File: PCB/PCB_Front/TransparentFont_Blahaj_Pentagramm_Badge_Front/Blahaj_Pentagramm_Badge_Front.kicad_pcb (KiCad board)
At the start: 2 copper layers, 79.8 x 79.8 mm, 13 parts

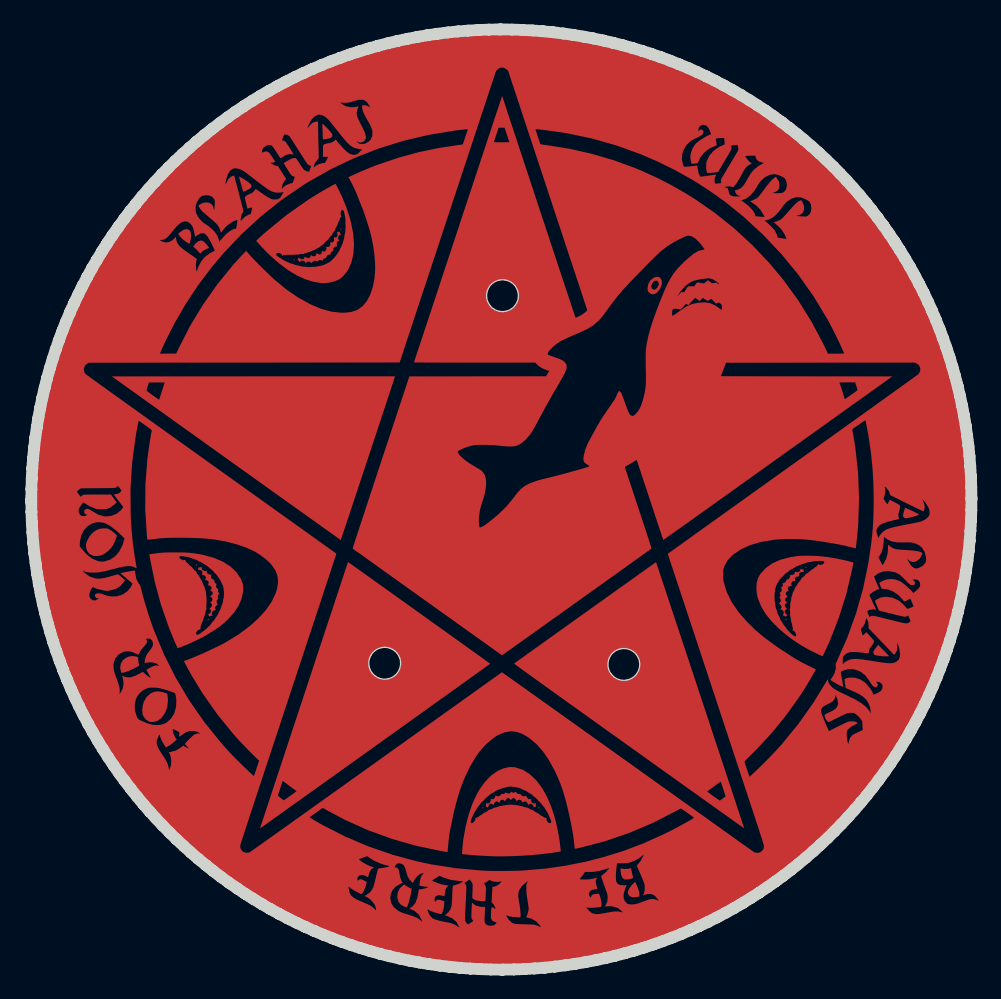
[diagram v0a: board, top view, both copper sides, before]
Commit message: Production Samples
TODO: Border for working sample to narrow.
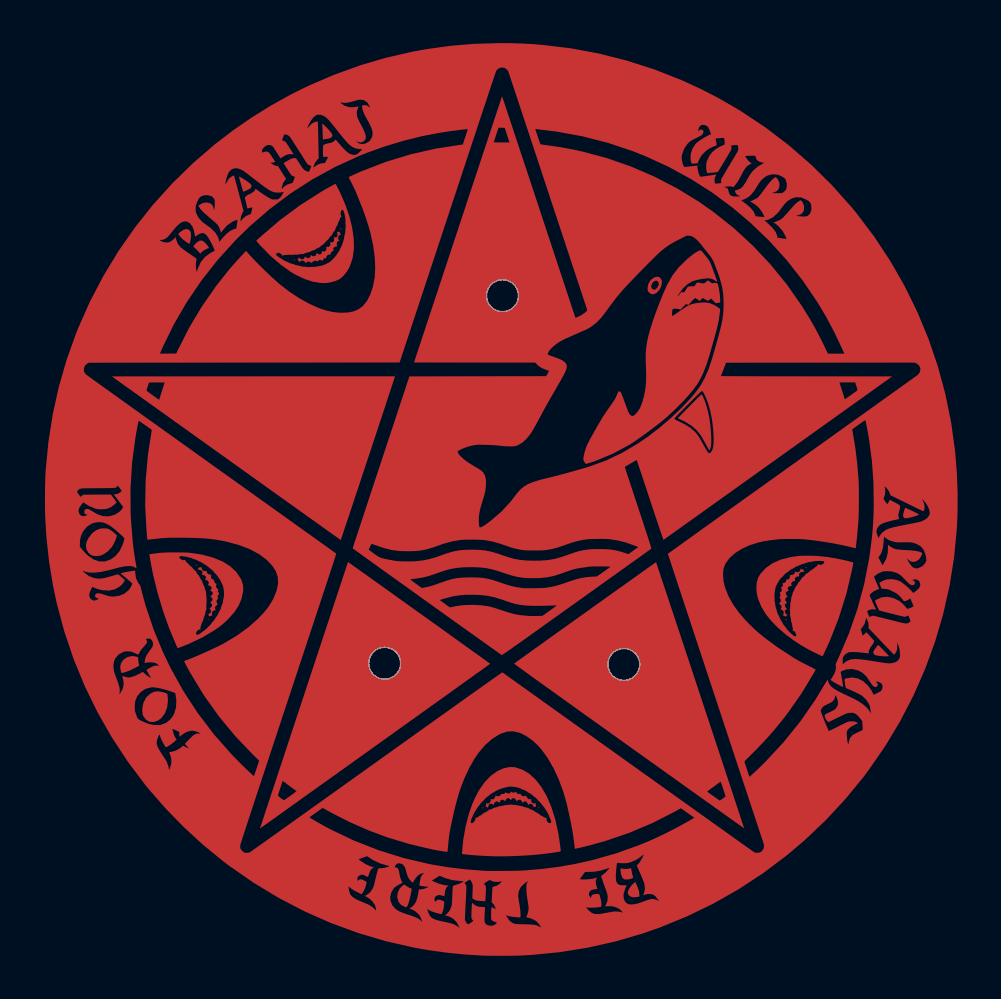
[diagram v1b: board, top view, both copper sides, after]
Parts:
- removed the ? at (100.0, 100.0) (x2)
- added ? (x14): , Graphics, F.Cu at (100.0, 100.0)
- added ? (x4): , Graphics, B.Cu at (100.0, 100.0)
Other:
- board outline removed

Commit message: Back corrections, Front Edge Cut bigger.
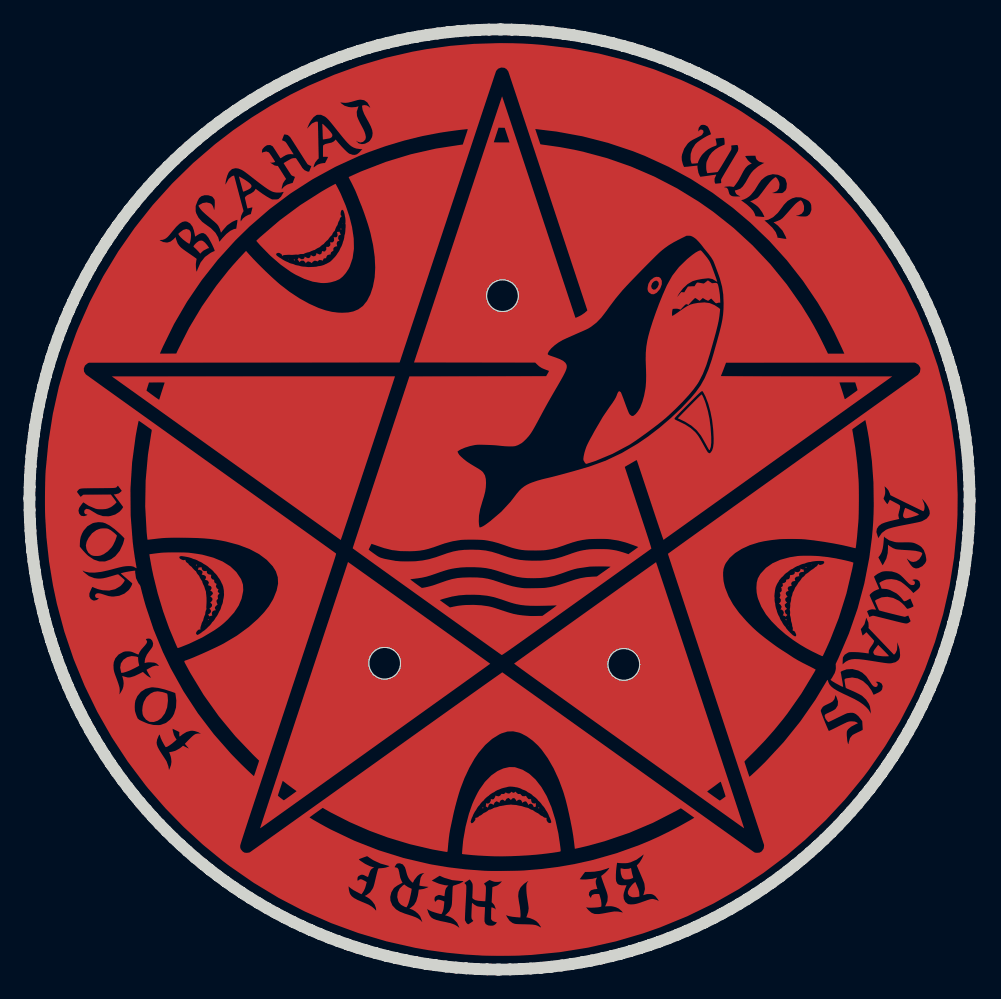
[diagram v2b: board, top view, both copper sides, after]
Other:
- board outline added: 79.8 x 79.8 mm
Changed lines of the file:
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@@
 			(drillshape 0)
 			(scaleselection 1)
-			(outputdirectory "production/")
+			(outputdirectory "production/Front_transparent/")
 		)
 	)
@@
 		(attr board_only exclude_from_pos_files exclude_from_bom)
 	)
+	(gr_poly
+		(pts
+			(xy 179.645 139.9) (xy 179.635 139.011) (xy 179.606 138.127) (xy 179.558 137.248) (xy 179.491 136.374)
+			(xy 179.406 135.505) (xy 179.302 134.642) (xy 179.179 133.785) (xy 179.039 132.934) (xy 178.881 132.088)
+			(xy 178.705 131.25) (xy 178.511 130.417) (xy 178.301 129.592) (xy 178.073 128.773) (xy 177.828 127.962)
+			(xy 177.567 127.158) (xy 177.289 126.361) (xy 176.996 125.573) (xy 176.686 124.792) (xy 176.36 124.02)
+			(xy 176.018 123.255) (xy 175.661 122.5) (xy 175.289 121.753) (xy 174.902 121.015) (xy 174.5 120.286)
+			(xy 174.083 119.567) (xy 173.652 118.857) (xy 173.206 118.158) (xy 172.747 117.468) (xy 172.273 116.788)
+			(xy 171.786 116.118) (xy 171.286 115.46) (xy 170.772 114.812) (xy 170.246 114.175) (xy 169.706 113.549)
+			(xy 169.154 112.934) (xy 168.589 112.331) (xy 168.012 111.74) (xy 167.424 111.161) (xy 166.823 110.594)
+			(xy 166.211 110.04) (xy 165.587 109.498) (xy 164.952 108.969) (xy 164.306 108.453) (xy 163.649 107.95)
+			(xy 162.982 107.461) (xy 162.304 106.985) (xy 161.616 106.523) (xy 160.918 106.075) (xy 160.21 105.641)
+			(xy 159.492 105.221) (xy 158.765 104.817) (xy 158.029 104.426) (xy 157.284 104.051) (xy 156.53 103.692)
+			(xy 155.767 103.347) (xy 154.996 103.019) (xy 154.217 102.706) (xy 153.43 102.409) (xy 152.635 102.128)
+			(xy 151.832 101.864) (xy 151.022 101.616) (xy 150.205 101.385) (xy 149.381 101.171) (xy 148.55 100.975)
+			(xy 147.712 100.795) (xy 146.868 100.634) (xy 146.018 100.49) (xy 145.162 100.365) (xy 144.3 100.257)
+			(xy 143.432 100.168) (xy 142.559 100.098) (xy 141.681 100.046) (xy 140.798 100.014) (xy 139.91 100)
+			(xy 139.745 100) (xy 138.856 100.01) (xy 137.972 100.039) (xy 137.093 100.087) (xy 136.219 100.154)
+			(xy 135.35 100.239) (xy 134.487 100.343) (xy 133.63 100.466) (xy 132.779 100.606) (xy 131.933 100.764)
+			(xy 131.095 100.94) (xy 130.262 101.134) (xy 129.437 101.344) (xy 128.618 101.572) (xy 127.807 101.817)
+			(xy 127.003 102.078) (xy 126.206 102.356) (xy 125.418 102.649) (xy 124.637 102.959) (xy 123.865 103.285)
+			(xy 123.1 103.627) (xy 122.345 103.984) (xy 121.598 104.356) (xy 120.86 104.743) (xy 120.131 105.145)
+			(xy 119.412 105.562) (xy 118.702 105.993) (xy 118.003 106.439) (xy 117.313 106.898) (xy 116.633 107.372)
+			(xy 115.963 107.859) (xy 115.305 108.359) (xy 114.657 108.873) (xy 114.02 109.399) (xy 113.394 109.939)
+			(xy 112.779 110.491) (xy 112.177 111.056) (xy 111.585 111.632) (xy 111.006 112.221) (xy 110.44 112.822)
+			(xy 109.885 113.434) (xy 109.343 114.058) (xy 108.814 114.693) (xy 108.298 115.339) (xy 107.795 115.996)
+			(xy 107.306 116.663) (xy 106.83 117.341) (xy 106.368 118.029) (xy 105.92 118.727) (xy 105.486 119.435)
+			(xy 105.066 120.153) (xy 104.662 120.88) (xy 104.272 121.616) (xy 103.896 122.361) (xy 103.537 123.115)
+			(xy 103.192 123.878) (xy 102.864 124.649) (xy 102.551 125.428) (xy 102.254 126.215) (xy 101.973 127.01)
+			(xy 101.709 127.813) (xy 101.461 128.623) (xy 101.23 129.44) (xy 101.016 130.264) (xy 100.82 131.095)
+			(xy 100.641 131.933) (xy 100.479 132.777) (xy 100.335 133.627) (xy 100.21 134.483) (xy 100.102 135.345)
+			(xy 100.013 136.213) (xy 99.943 137.086) (xy 99.891 137.964) (xy 99.859 138.847) (xy 99.845 139.735)
+			(xy 99.845 139.9) (xy 99.855 140.789) (xy 99.884 141.673) (xy 99.932 142.552) (xy 99.999 143.426)
+			(xy 100.084 144.295) (xy 100.188 145.158) (xy 100.311 146.015) (xy 100.451 146.866) (xy 100.609 147.711)
+			(xy 100.785 148.55) (xy 100.979 149.383) (xy 101.189 150.208) (xy 101.417 151.027) (xy 101.662 151.838)
+			(xy 101.923 152.642) (xy 102.201 153.438) (xy 102.494 154.227) (xy 102.804 155.008) (xy 103.13 155.78)
+			(xy 103.472 156.545) (xy 103.829 157.3) (xy 104.201 158.047) (xy 104.588 158.785) (xy 104.99 159.513)
+			(xy 105.407 160.233) (xy 105.838 160.942) (xy 106.284 161.642) (xy 106.743 162.332) (xy 107.217 163.012)
+			(xy 107.704 163.681) (xy 108.204 164.34) (xy 108.718 164.988) (xy 109.244 165.625) (xy 109.784 166.251)
+			(xy 110.336 166.866) (xy 110.901 167.468) (xy 111.477 168.059) (xy 112.066 168.639) (xy 112.667 169.205)
+			(xy 113.279 169.76) (xy 113.903 170.302) (xy 114.538 170.831) (xy 115.184 171.347) (xy 115.841 171.85)
+			(xy 116.508 172.339) (xy 117.186 172.815) (xy 117.874 173.277) (xy 118.572 173.725) (xy 119.28 174.159)
+			(xy 119.998 174.579) (xy 120.725 174.983) (xy 121.461 175.373) (xy 122.206 175.748) (xy 122.96 176.108)
+			(xy 123.723 176.453) (xy 124.494 176.781) (xy 125.273 177.094) (xy 126.06 177.391) (xy 126.855 177.672)
+			(xy 127.658 177.936) (xy 128.468 178.184) (xy 129.285 178.415) (xy 130.109 178.629) (xy 130.94 178.825)
+			(xy 131.778 179.004) (xy 132.622 179.166) (xy 133.472 179.31) (xy 134.328 179.435) (xy 135.19 179.543)
+			(xy 136.058 179.632) (xy 136.931 179.702) (xy 137.809 179.754) (xy 138.692 179.786) (xy 139.58 179.8)
+			(xy 139.745 179.8) (xy 140.634 179.79) (xy 141.518 179.761) (xy 142.397 179.713) (xy 143.271 179.646)
+			(xy 144.14 179.561) (xy 145.003 179.457) (xy 145.86 179.334) (xy 146.711 179.194) (xy 147.557 179.036)
+			(xy 148.395 178.86) (xy 149.228 178.666) (xy 150.053 178.456) (xy 150.872 178.228) (xy 151.683 177.983)
+			(xy 152.487 177.722) (xy 153.283 177.444) (xy 154.072 177.151) (xy 154.853 176.84) (xy 155.625 176.515)
+			(xy 156.39 176.173) (xy 157.145 175.816) (xy 157.892 175.444) (xy 158.63 175.057) (xy 159.358 174.655)
+			(xy 160.078 174.238) (xy 160.787 173.807) (xy 161.487 173.361) (xy 162.177 172.902) (xy 162.857 172.428)
+			(xy 163.527 171.941) (xy 164.185 171.441) (xy 164.833 170.927) (xy 165.47 170.401) (xy 166.096 169.861)
+			(xy 166.711 169.309) (xy 167.313 168.744) (xy 167.905 168.167) (xy 168.484 167.579) (xy 169.05 166.978)
+			(xy 169.605 166.366) (xy 170.147 165.742) (xy 170.676 165.107) (xy 171.192 164.461) (xy 171.695 163.804)
+			(xy 172.184 163.137) (xy 172.66 162.459) (xy 173.122 161.771) (xy 173.57 161.073) (xy 174.004 160.365)
+			(xy 174.424 159.647) (xy 174.828 158.92) (xy 175.218 158.184) (xy 175.593 157.439) (xy 175.953 156.685)
+			(xy 176.298 155.922) (xy 176.626 155.151) (xy 176.939 154.372) (xy 177.236 153.585) (xy 177.517 152.79)
+			(xy 177.781 151.987) (xy 178.029 151.177) (xy 178.26 150.36) (xy 178.474 149.536) (xy 178.67 148.705)
+			(xy 178.849 147.867) (xy 179.011 147.023) (xy 179.155 146.173) (xy 179.28 145.317) (xy 179.388 144.455)
+			(xy 179.477 143.587) (xy 179.547 142.714) (xy 179.599 141.836) (xy 179.631 140.953) (xy 179.645 140.065)
+			(xy 179.645 139.9)
+		)
+		(stroke
+			(width 1)
+			(type solid)
+		)
+		(fill none)
+		(layer "Edge.Cuts")
+	)
 )

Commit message: Production ready commit
Production Version 3 commit
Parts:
- removed the ? at (100.0, 100.0) (x2)
- added ? (x32): , Graphics, F.Cu at (100.0, 100.0)
- added ? (x3): , Graphics, F.Cu at (108.5, 110.9)
- added ? (x10): , Graphics, B.Cu at (100.0, 100.0)
- added ?: , Graphics, B.Cu at (108.5, 110.9)
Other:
- board size 79.8 x 79.8 mm -> 80 x 79.8 mm
